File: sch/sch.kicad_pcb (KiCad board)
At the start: 2 copper layers, 99.1 x 49.5 mm, 66 parts, among them P1 CONN_01X02, P10 CONN_1, P11 CONN_1, P2 CONN_02X05, P3 CONN_01X06, P4 CONN_01X06, P5 BNC, P6 Digital, P7 Analog, P8 CONN_1, P9 CONN_1, U1 PT4115, U10 DS18B20, U11 DS18B20, U12 DS18B20, U13 DS18B20, U2 PT4115, U3 PT4115, U4 PT4115, U5 PT4115, U6 PT4115, U7 LM324, U9 LM7805CT

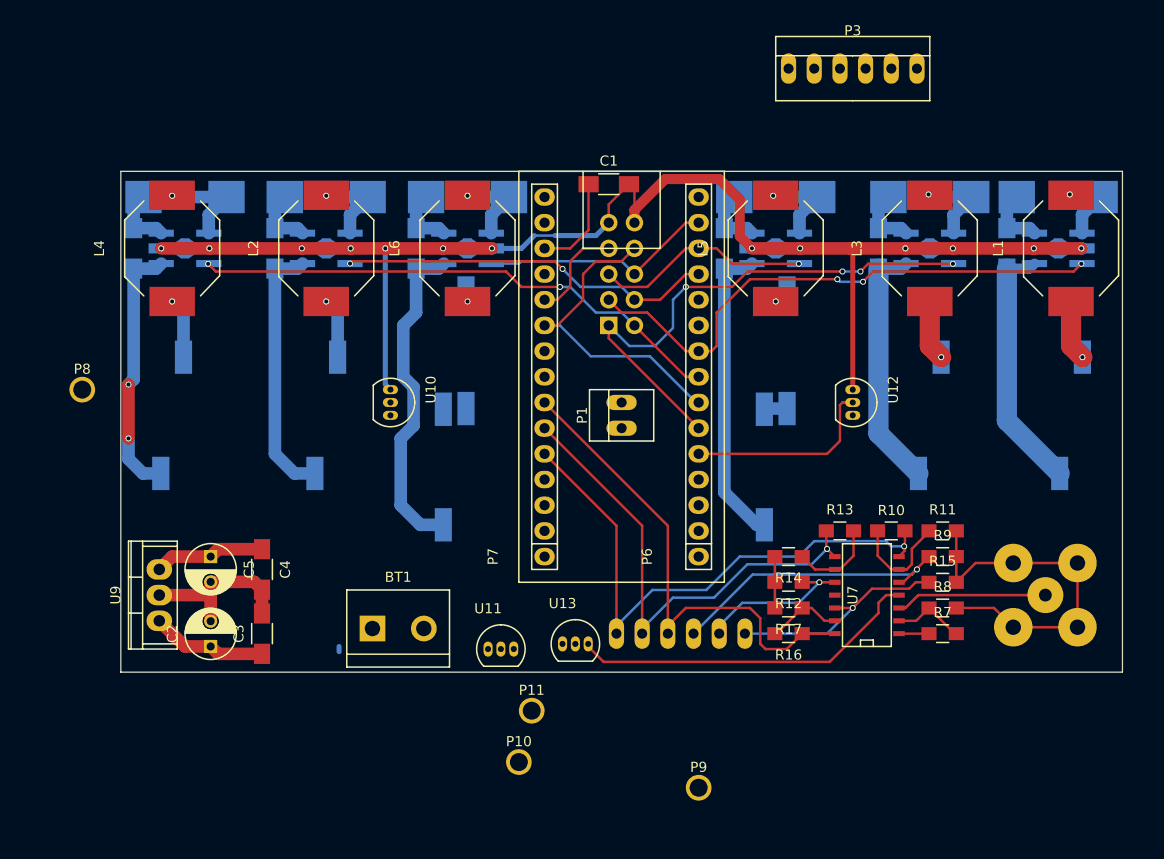
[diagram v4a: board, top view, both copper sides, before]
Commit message: Changed some connections to make layout easier
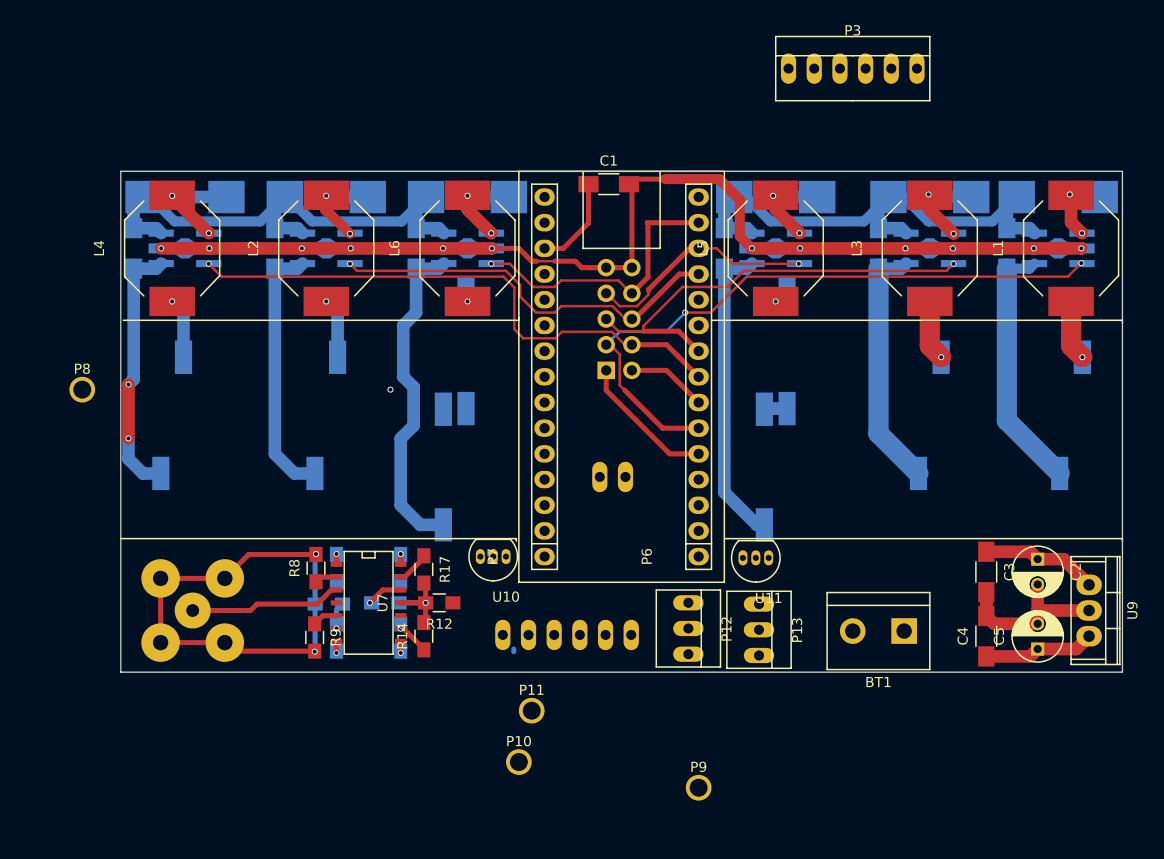
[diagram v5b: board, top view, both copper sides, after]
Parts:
- removed U12, U13: DS18B20, TO_SOT_Packages_THT:TO-92_Inline_Narrow_Oval
- added P12: CONN_01X03, Connect:PINHEAD1-3, F.Cu at (129.8, 110.0)
- added P13: CONN_01X03, Connect:PINHEAD1-3, F.Cu at (136.8, 110.1)
- P1, R10, R11, R13, R15, R16, R7: moved to B.Cu
- moved U9 92.0 mm to (169.4, 108.2), turned to 270 degrees
- moved P5 84.3 mm to (80.8, 108.2)
- moved C5 82.3 mm to (164.3, 112.0), turned to 90 degrees
- moved C2 82.2 mm to (164.3, 103.1), turned to 270 degrees
- moved C4 71.9 mm to (159.3, 110.7), turned to 90 degrees
- moved C3 71.9 mm to (159.3, 104.4), turned to 270 degrees
- moved R9 62.6 mm to (92.8, 110.9), turned to 270 degrees
- moved R8 62.1 mm to (93.0, 104.0), turned to 90 degrees
- moved R11 61.1 mm to (94.2, 107.6), turned to 180 degrees
- moved R7 60.3 mm to (95.0, 104.0), turned to 270 degrees
- moved R10 55.9 mm to (95.0, 110.9), turned to 90 degrees
- moved R15 55.2 mm to (99.8, 107.4)
- moved U7 49.0 mm to (98.3, 107.4), turned to 270 degrees
- moved BT1 47.5 mm to (148.6, 110.2), turned to 180 degrees
- moved R13 44.7 mm to (101.3, 110.9), turned to 90 degrees
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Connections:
- P2 pad 1: /3(**) -> /2
- P2 pad 2: /5(**) -> /4
- P2 pad 3: /6(**) -> /3(**)
- P2 pad 4: /9(**) -> /5(**)
- P2 pad 5: /10(**/SS) -> /6(**)
- P2 pad 6: /11(**/MISO) -> /9(**)
- P2 pad 7: /2 -> /10(**/SS)
- P2 pad 8: /4 -> /11(**/MISO)
- P4 pad 1: /12(MOSI) -> /A6
- P4 pad 2: /13(SCK) -> /A7
- P4 pad 3: /A0 -> /A5
- P7 pad 10: /4 -> /A2
- P7 pad 11: /2 -> /A1
- P7 pad 5: /12(MOSI) -> /A7
- P7 pad 6: /13(SCK) -> /A6
- P7 pad 7: /A0 -> /A5
- R10 pad 1: /12(MOSI) -> /A7
- R13 pad 1: /13(SCK) -> /A6
- R16 pad 1: /A0 -> /A5
- U1 pad 3: /6(**) -> /3(**)
- U10 pad 2: /7 -> Net-(P12-Pad2)
- U11 pad 2: /8 -> Net-(P13-Pad2)
- U3 pad 3: /3(**) -> /6(**)
- U7 pad 14: /A0 -> /A5
- U7 pad 7: /12(MOSI) -> /A7
- U7 pad 8: /13(SCK) -> /A6
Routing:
- net +BATT: track 50.0 -> 113.9 mm
- net /12(MOSI): track 56.6 -> 0.00 mm, vias 1 -> 0
- net /A0: track 49.7 -> 0.00 mm
- net /13(SCK): track 49.4 -> 0.00 mm, vias 1 -> 0
- net +5V: track 45.9 -> 11.5 mm
- net /O_MEAS: track 28.9 -> 2.49 mm, vias 1 -> 0
- net /4: track 32.2 -> 8.43 mm
- net /O_CAL1: track 22.1 -> 3.75 mm
- net /O_CAL0: track 15.7 -> 0.00 mm, vias 1 -> 0
- net /2: track 29.4 -> 13.7 mm
- net GND: track 193.5 -> 180.9 mm, vias 14 -> 15
- net /3(**): track 53.8 -> 64.9 mm, vias 4 -> 2
- net /6(**): track 54.6 -> 44.3 mm, vias 3 -> 1
- net Net-(R10-Pad2): track 11.6 -> 2.66 mm, vias 0 -> 1
- net /11(**/MISO): track 23.2 -> 28.4 mm, vias 0 -> 1
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
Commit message: Initial version done
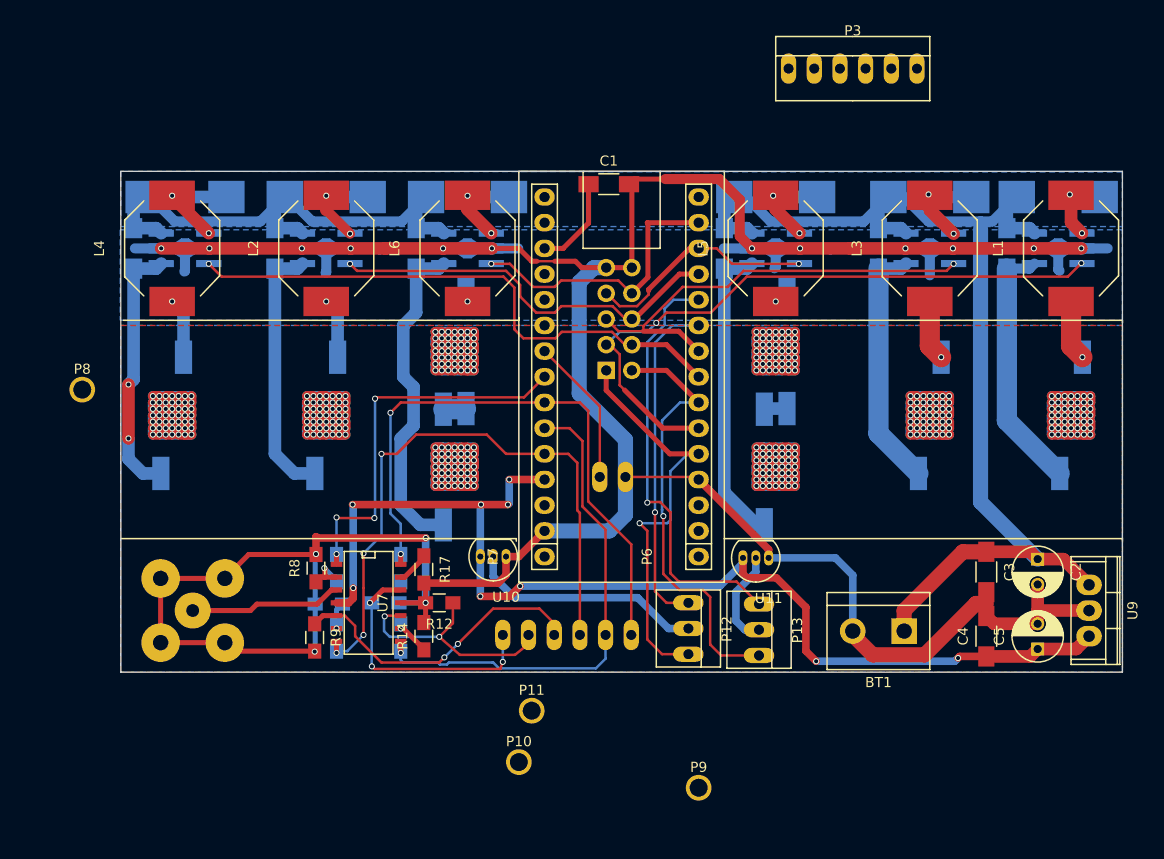
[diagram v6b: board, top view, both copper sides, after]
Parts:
- D4: footprint sch:lumiled-2-LAMBERTIAN -> lumiled-2-LAMBERTIAN
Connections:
- P4 pad 1: /A6 -> /A5
- P4 pad 2: /A7 -> /A6
- P4 pad 3: /A5 -> /A7
- P6 pad 3: /Reset -> Net-(P6-Pad3)
- P7 pad 3: /Reset -> Net-(P7-Pad3)
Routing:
- net (no net): track 0.25 -> 254.0 mm, vias 1 -> 392
- net GND: track 180.9 -> 388.2 mm, vias 15 -> 16
- net +5V: track 11.5 -> 112.9 mm, vias 0 -> 9
- net /A7: track 1.32 -> 61.7 mm, vias 1 -> 4
- net /A5: track 1.06 -> 59.7 mm, vias 1 -> 2
- net /A6: track 1.32 -> 50.1 mm
- net +BATT: track 113.9 -> 162.2 mm
- net /8: track 0.51 -> 42.9 mm, vias 0 -> 1
- net /A4: track 1.06 -> 38.0 mm, vias 1 -> 4
- net /4: track 8.43 -> 43.6 mm, vias 0 -> 1
- net /7: track 0.00 -> 33.4 mm, vias 0 -> 1
- net /O_MEAS: track 2.49 -> 30.5 mm, vias 0 -> 2
- net /2: track 13.7 -> 41.7 mm, vias 0 -> 1
- net /O_CAL0: track 0.00 -> 23.5 mm, vias 0 -> 2
- net Net-(P12-Pad2): track 0.00 -> 23.4 mm
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- added copper zone on B.Cu, net +BATT
- added copper zone on F.Cu, net +BATT
- added copper zone on B.Cu, net GND

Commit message: Some minor fixes
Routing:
- net +BATT: track 162.2 -> 179.9 mm, vias 0 -> 8
- net Net-(R16-Pad2): track 3.28 -> 3.74 mm, vias 0 -> 1
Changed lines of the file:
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@@
   (general
     (links 162)
-    (no_connects 2)
+    (no_connects 0)
     (area 73.609999 64.719999 172.770001 114.350001)
     (thickness 1.6)
     (drawings 24)
-    (tracks 1448)
+    (tracks 1468)
     (zones 0)
     (modules 66)
@@
   (segment (start 117.4115 72.39) (end 115.57 72.39) (width 0.5) (layer F.Cu) (net 19))
   (segment (start 119.92 69.8815) (end 117.4115 72.39) (width 0.5) (layer F.Cu) (net 19))
+  (segment (start 158.75 101.886) (end 158.75 82.55) (width 1.5) (layer F.Cu) (net 21))
+  (via (at 158.75 82.55) (size 0.6) (drill 0.4) (layers F.Cu B.Cu) (net 21))
+  (segment (start 158.75 82.55) (end 158.75 81.28) (width 1.5) (layer B.Cu) (net 21))
+  (via (at 158.75 81.28) (size 0.6) (drill 0.4) (layers F.Cu B.Cu) (net 21))
+  (segment (start 158.845 70.39) (end 161.29 70.39) (width 1.5) (layer B.Cu) (net 21))
+  (segment (start 158.75 70.485) (end 158.75 81.28) (width 1.5) (layer B.Cu) (net 21))
+  (segment (start 158.845 70.39) (end 158.75 70.485) (width 1.5) (layer B.Cu) (net 21))
+  (via (at 157.48 82.55) (size 0.6) (drill 0.4) (layers F.Cu B.Cu) (net 21))
+  (segment (start 157.48 81.28) (end 158.75 81.28) (width 1.5) (layer B.Cu) (net 21))
+  (via (at 157.48 81.28) (size 0.6) (drill 0.4) (layers F.Cu B.Cu) (net 21))
+  (segment (start 157.48 82.55) (end 157.48 81.28) (width 1.5) (layer B.Cu) (net 21))
+  (segment (start 158.75 101.886) (end 159.258 102.394) (width 1.5) (layer F.Cu) (net 21))
+  (segment (start 86.995 81.28) (end 86.995 82.55) (width 1.5) (layer B.Cu) (net 21))
+  (via (at 86.995 81.28) (size 0.6) (drill 0.4) (layers F.Cu B.Cu) (net 21))
+  (via (at 86.995 82.55) (size 0.6) (drill 0.4) (layers F.Cu B.Cu) (net 21))
+  (segment (start 85.725 82.55) (end 85.725 81.28) (width 1.5) (layer B.Cu) (net 21))
+  (via (at 85.725 81.28) (size 0.6) (drill 0.4) (layers F.Cu B.Cu) (net 21))
+  (segment (start 86.995 81.28) (end 86.995 70.195) (width 1.5) (layer B.Cu) (net 21))
+  (segment (start 85.725 81.28) (end 86.995 81.28) (width 1.5) (layer B.Cu) (net 21))
+  (via (at 85.725 82.55) (size 0.6) (drill 0.4) (layers F.Cu B.Cu) (net 21))
   (segment (start 151.13 110.236) (end 151.13 108.204) (width 1.5) (layer F.Cu) (net 21))
   (segment (start 156.94 102.394) (end 159.258 102.394) (width 1.5) (layer F.Cu) (net 21))
   (segment (start 151.13 108.204) (end 156.94 102.394) (width 1.5) (layer F.Cu) (net 21))
-  (segment (start 158.6865 70.485) (end 158.6865 97.4725) (width 1.5) (layer B.Cu) (net 21))
-  (segment (start 158.6865 69.723) (end 158.6865 70.485) (width 1) (layer B.Cu) (net 21))
-  (segment (start 158.6865 97.4725) (end 164.338 103.124) (width 1.5) (layer B.Cu) (net 21))
   (segment (start 149.57 67.31) (end 151.13 67.31) (width 1) (layer B.Cu) (net 21))
   (segment (start 151.13 67.31) (end 153.543 69.723) (width 1) (layer B.Cu) (net 21))
@@
   (segment (start 75.91 67.31) (end 76.581 67.31) (width 1) (layer B.Cu) (net 21))
   (segment (start 76.581 67.31) (end 78.994 69.723) (width 1) (layer B.Cu) (net 21))
-  (segment (start 87.467 69.723) (end 89.88 67.31) (width 1) (layer B.Cu) (net 21))
+  (segment (start 87.467 69.723) (end 86.995 70.195) (width 1) (layer B.Cu) (net 21))
+  (segment (start 86.995 70.195) (end 89.88 67.31) (width 1) (layer B.Cu) (net 21))
   (segment (start 78.994 69.723) (end 87.467 69.723) (width 1) (layer B.Cu) (net 21))
   (segment (start 159.258 102.394) (end 163.608 102.394) (width 1.25) (layer F.Cu) (net 21))
@@
   (via (at 98.298 107.442) (size 0.6) (drill 0.4) (layers F.Cu B.Cu) (net 40))
   (segment (start 99.568 106.172) (end 98.298 107.442) (width 0.5) (layer F.Cu) (net 40))
+  (via (at 101.346 104.902) (size 0.6) (drill 0.4) (layers F.Cu B.Cu) (net 41))
+  (segment (start 101.346 104.902) (end 101.346 105.363) (width 0.25) (layer B.Cu) (net 41))
   (segment (start 101.346 104.902) (end 101.727 104.902) (width 0.5) (layer F.Cu) (net 41))
   (segment (start 101.727 104.902) (end 103.632 102.997) (width 0.5) (layer F.Cu) (net 41))
@@
     (connect_pads (clearance 0.2))
     (min_thickness 0.254)
-    (keepout (tracks not_allowed) (vias not_allowed) (copperpour not_allowed))
+    (keepout (tracks allowed) (vias allowed) (copperpour not_allowed))
     (fill (arc_segments 16) (thermal_gap 0.508) (thermal_bridge_width 0.508))
     (polygon
@@
     (polygon
       (pts
-        (xy 73.66 80.01) (xy 172.72 80.01) (xy 172.72 114.3) (xy 73.66 114.3)
+        (xy 73.66 71.12) (xy 172.72 71.12) (xy 172.72 114.3) (xy 73.66 114.3)
       )
     )

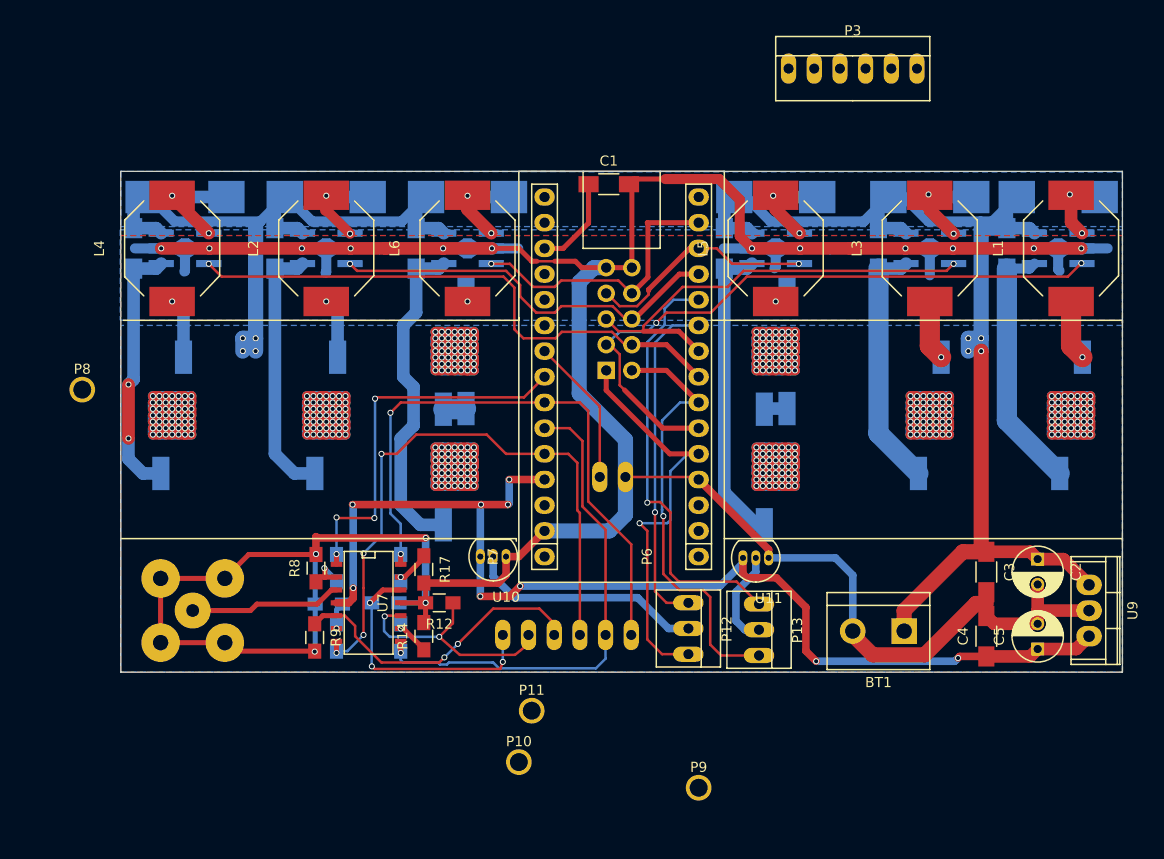
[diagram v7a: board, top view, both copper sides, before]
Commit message: Fixed silkscreen and moved bnc connector so that silkscreen is on the board
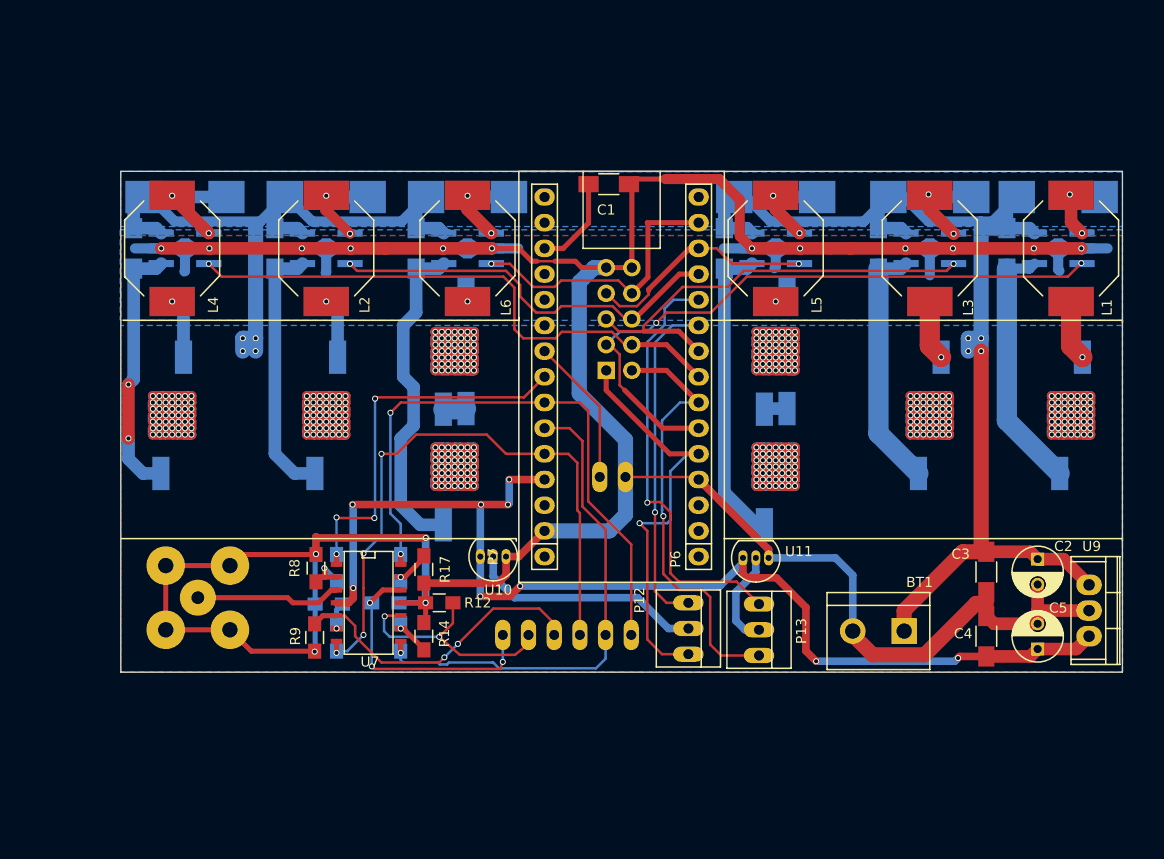
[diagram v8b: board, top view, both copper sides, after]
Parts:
- removed P10, P11, P8, P9: CONN_1, Socket_Arduino_Nano:1pin_Nano
- removed P3: CONN_01X06, Connect:PINHEAD1-6
- D8: footprint Diodes_SMD:DO-214AB_Handsoldering -> DO-214AB_Handsoldering
- moved P5 1.37 mm to (81.3, 106.9)
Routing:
- net GND: track 388.2 -> 387.2 mm
